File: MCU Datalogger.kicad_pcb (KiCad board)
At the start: 2 copper layers, 49.5 x 26.5 mm, 30 parts, among them J1 Conn_01x04_Pin, J2 Conn_01x04_Pin, J3 Conn_01x09_Pin, J4 Conn_02x03_Odd_Even, U1 24LC1025, U2 24LC1025, U3 DS1337S_, U4 ATMEGA328P-AU, Y1 16 MHz, Y2 32.768kHz

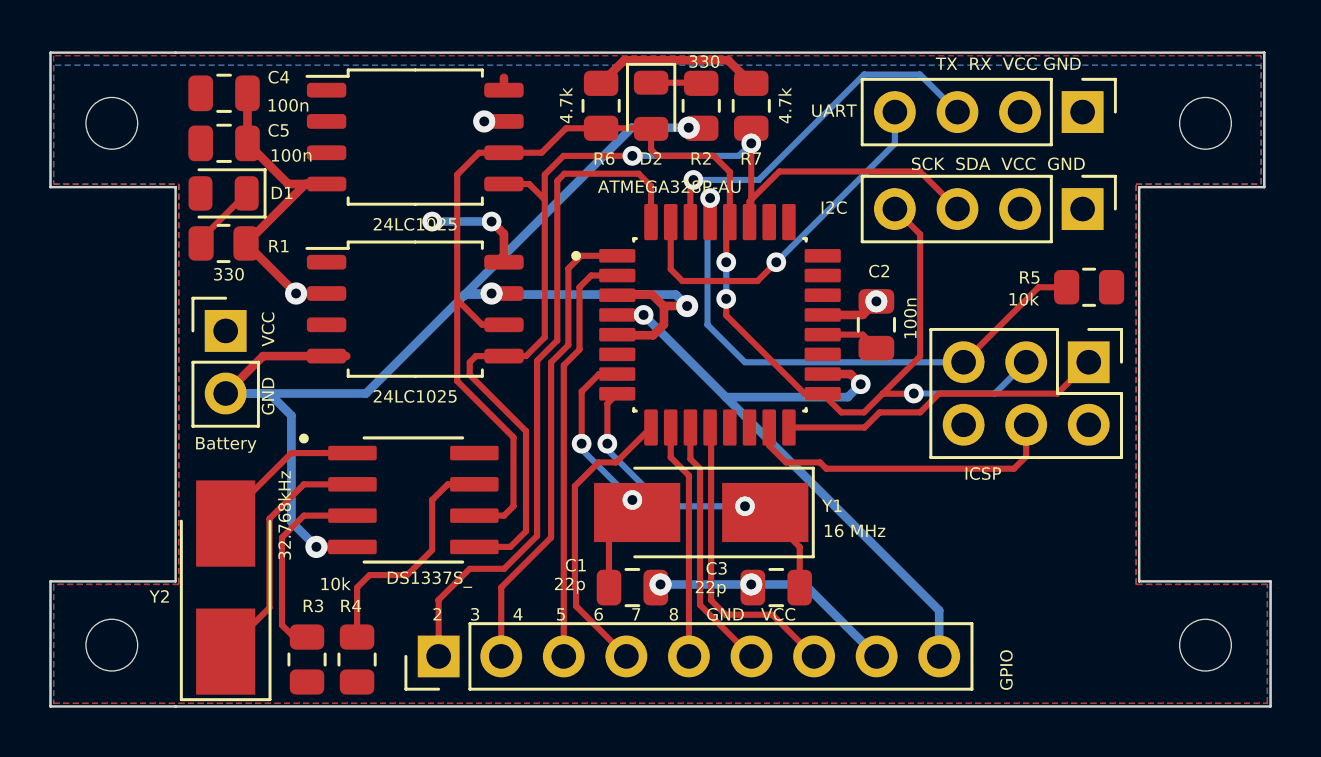
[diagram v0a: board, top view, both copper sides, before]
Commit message: 4-layer PCB completed
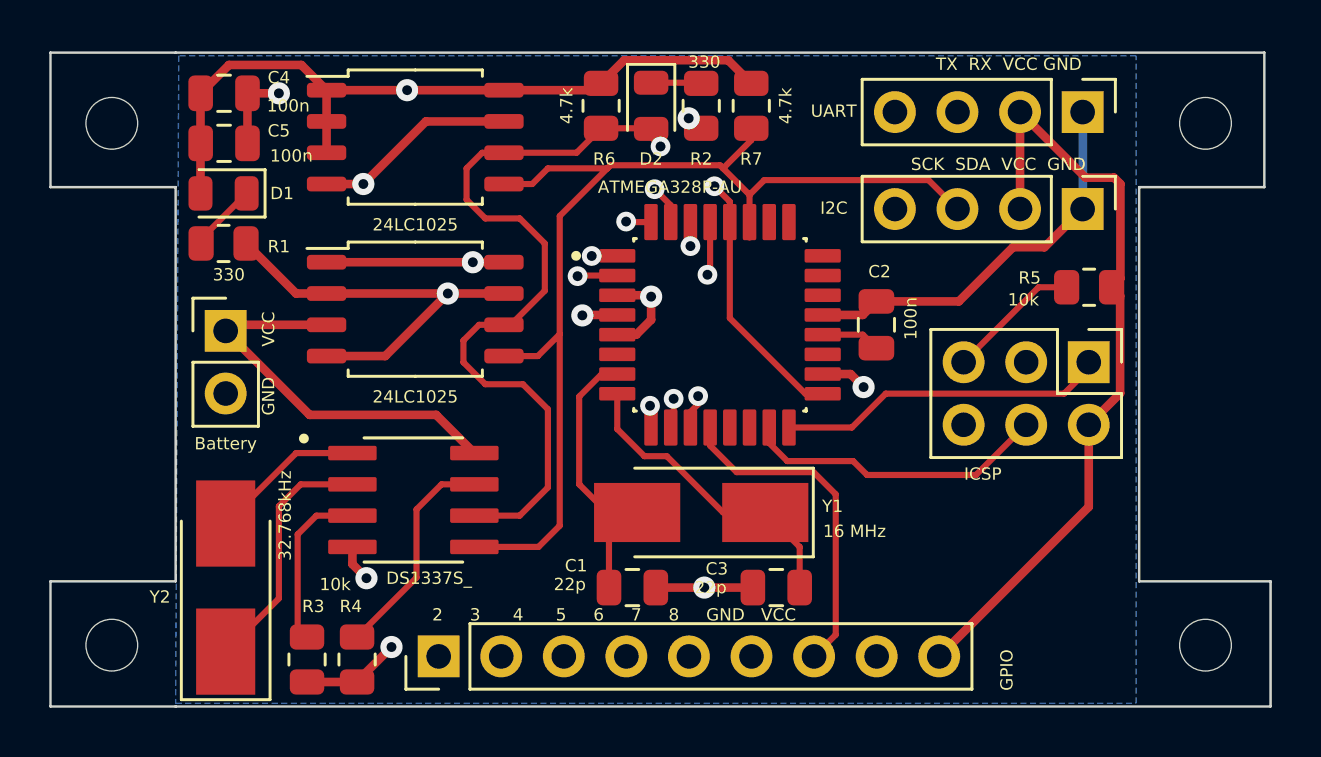
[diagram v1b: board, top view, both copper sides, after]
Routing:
- net /Vcc: track 39.5 -> 133.5 mm, vias 4 -> 5
- net GND: track 83.0 -> 55.2 mm, vias 9 -> 7
- net /D6: track 9.60 -> 17.0 mm, vias 0 -> 1
- net /D7: track 10.3 -> 17.2 mm, vias 0 -> 1
- net /D2: track 27.7 -> 23.0 mm, vias 0 -> 1
- net /D4: track 17.0 -> 20.9 mm, vias 0 -> 1
- net /RESET: track 22.0 -> 19.5 mm
- net /D3: track 19.1 -> 21.3 mm, vias 0 -> 1
- net /D5: track 11.9 -> 14.0 mm, vias 0 -> 1
- net /TX: track 14.8 -> 12.7 mm
- net /D8: track 12.2 -> 13.6 mm
- net /~{INTA}: track 8.00 -> 6.86 mm
- net Net-(U4-PB7): track 13.5 -> 12.5 mm, vias 2 -> 0
- net /SCK: track 60.6 -> 61.7 mm, vias 3 -> 2
- net /SQW: track 9.69 -> 8.95 mm
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- added copper zone on In2.Cu, net /Vcc
- removed copper zone on F.Cu, net /Vcc
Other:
- copper layers 2 -> 4

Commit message: board charasteristics added
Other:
- board text added: "4"
- board text removed: "2"
- board text removed: "Afterall, there are some clearence violations that must be corrected"
- board text removed: "CORRECTED"
- board text removed: "Unfortunately Vcc label is not defined as POWER net class so that Vcc track width was set as default (0.25mm). After the DRC process, the net class definitions checked and reorganized. Labels that entered by users should write with {dblquote}/{dblquote} prefix. For example /Vcc ."
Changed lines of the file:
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@@
       (drillshape 0)
       (scaleselection 1)
-      (outputdirectory "MCU_Datalogger_Gerbers/")
+      (outputdirectory "4_layer_MCU_Datalogger_Gerbers/")
     )
   )
@@
   (gr_line (start 123.952 76.454) (end 129.032 76.454)
     (stroke (width 0.1) (type default)) (layer "Edge.Cuts"))
-  (gr_rect (start 121.158 22.86) (end 194.818 47.371)
-    (stroke (width 0.15) (type default)) (fill none) (layer "User.1"))
   (gr_rect (start 129.00438 50.36596) (end 168.23842 76.42819)
     (stroke (width 0.1) (type default)) (fill none) (layer "User.1"))
@@
     (effects (font (size 0.5 0.5) (thickness 0.0625)) (justify left bottom))
   )
-  (gr_text "49.5300 mm x 26.5430 mm" (at 153.041143 104.447) (layer "User.1")
+  (gr_text "None" (at 142.113 106.192) (layer "User.1")
     (effects (font (size 1.5 1.5) (thickness 0.2)) (justify left top))
   )
-  (gr_text "None" (at 153.041143 112.361) (layer "User.1")
+  (gr_text "No" (at 142.113 114.106) (layer "User.1")
     (effects (font (size 1.5 1.5) (thickness 0.2)) (justify left top))
   )
-  (gr_text "No" (at 212.141138 116.318) (layer "User.1")
+  (gr_text "1.6000 mm" (at 201.212995 94.321) (layer "User.1")
     (effects (font (size 1.5 1.5) (thickness 0.2)) (justify left top))
   )
-  (gr_text "Copper Finish: " (at 120.384 112.361) (layer "User.1")
+  (gr_text "Board Thickness: " (at 176.270138 94.321) (layer "User.1")
     (effects (font (size 1.5 1.5) (thickness 0.2)) (justify left top))
   )
-  (gr_text "BOARD CHARACTERISTICS" (at 119.634 94.996) (layer "User.1")
-    (effects (font (size 2 2) (thickness 0.4)) (justify left top))
-  )
-  (gr_text "Unfortunately Vcc label is not defined as POWER net class\nso that Vcc track width was set as default (0.25mm). \nAfter the DRC process, the net class definitions checked and\nreorganized. \n\nLabels that entered by users should write with {dblquote}/{dblquote} prefix.\nFor example /Vcc ." (at 122.301 40.259) (layer "User.1")
-    (effects (font (size 1.5 1.5) (thickness 0.1875)) (justify left bottom))
-  )
-  (gr_text "" (at 187.198281 104.447) (layer "User.1")
+  (gr_text "0.3000 mm" (at 201.212995 102.235) (layer "User.1")
     (effects (font (size 1.5 1.5) (thickness 0.2)) (justify left top))
   )
-  (gr_text "Edge card connectors: " (at 120.384 120.275) (layer "User.1")
+  (gr_text "Min hole diameter: " (at 176.270138 102.235) (layer "User.1")
     (effects (font (size 1.5 1.5) (thickness 0.2)) (justify left top))
   )
-  (gr_text "Plated Board Edge: " (at 187.198281 116.318) (layer "User.1")
+  (gr_text "49.5300 mm x 26.5430 mm" (at 142.113 98.278) (layer "User.1")
     (effects (font (size 1.5 1.5) (thickness 0.2)) (justify left top))
   )
-  (gr_text "Copper Layer Count: " (at 120.384 100.49) (layer "User.1")
+  (gr_text "Impedance Control: " (at 176.270138 106.192) (layer "User.1")
     (effects (font (size 1.5 1.5) (thickness 0.2)) (justify left top))
   )
-  (gr_text "No" (at 212.141138 112.361) (layer "User.1")
+  (gr_text "0.2000 mm / 0.0000 mm" (at 142.113 102.235) (layer "User.1")
     (effects (font (size 1.5 1.5) (thickness 0.2)) (justify left top))
   )
-  (gr_text "0.3000 mm" (at 212.141138 108.404) (layer "User.1")
+  (gr_text "Plated Board Edge: " (at 176.270138 110.149) (layer "User.1")
     (effects (font (size 1.5 1.5) (thickness 0.2)) (justify left top))
   )
-  (gr_text "2" (at 153.041143 100.49) (layer "User.1")
+  (gr_text "" (at 201.212995 98.278) (layer "User.1")
     (effects (font (size 1.5 1.5) (thickness 0.2)) (justify left top))
   )
-  (gr_text "1.6000 mm" (at 212.141138 100.49) (layer "User.1")
+  (gr_text "Copper Layer Count: " (at 109.455857 94.321) (layer "User.1")
     (effects (font (size 1.5 1.5) (thickness 0.2)) (justify left top))
   )
-  (gr_text "Min track/spacing: " (at 120.384 108.404) (layer "User.1")
+  (gr_text "Min track/spacing: " (at 109.455857 102.235) (layer "User.1")
     (effects (font (size 1.5 1.5) (thickness 0.2)) (justify left top))
   )
-  (gr_text "No" (at 153.041143 120.275) (layer "User.1")
-    (effects (font (size 1.5 1.5) (thickness 0.2)) (justify left top))
+  (gr_text "BOARD CHARACTERISTICS" (at 108.705857 88.827) (layer "User.1")
+    (effects (font (size 2 2) (thickness 0.4)) (justify left top))
   )
-  (gr_text "Min hole diameter: " (at 187.198281 108.404) (layer "User.1")
+  (gr_text "No" (at 201.212995 106.192) (layer "User.1")
     (effects (font (size 1.5 1.5) (thickness 0.2)) (justify left top))
   )
-  (gr_text "" (at 212.141138 104.447) (layer "User.1")
+  (gr_text "Board overall dimensions: " (at 109.455857 98.278) (layer "User.1")
     (effects (font (size 1.5 1.5) (thickness 0.2)) (justify left top))
   )
-  (gr_text "No" (at 153.041143 116.318) (layer "User.1")
+  (gr_text "Castellated pads: " (at 109.455857 110.149) (layer "User.1")
     (effects (font (size 1.5 1.5) (thickness 0.2)) (justify left top))
   )
-  (gr_text "Impedance Control: " (at 187.198281 112.361) (layer "User.1")
+  (gr_text "" (at 176.270138 98.278) (layer "User.1")
     (effects (font (size 1.5 1.5) (thickness 0.2)) (justify left top))
   )
-  (gr_text "Afterall, there are some clearence violations that must be \ncorrected" (at 122.174 44.958) (layer "User.1")
-    (effects (font (size 1.5 1.5) (thickness 0.1875)) (justify left bottom))
-  )
-  (gr_text "Board Thickness: " (at 187.198281 100.49) (layer "User.1")
+  (gr_text "No" (at 142.113 110.149) (layer "User.1")
     (effects (font (size 1.5 1.5) (thickness 0.2)) (justify left top))
   )
-  (gr_text "Castellated pads: " (at 120.384 116.318) (layer "User.1")
+  (gr_text "Copper Finish: " (at 109.455857 106.192) (layer "User.1")
     (effects (font (size 1.5 1.5) (thickness 0.2)) (justify left top))
   )
-  (gr_text "Board overall dimensions: " (at 120.384 104.447) (layer "User.1")
+  (gr_text "Edge card connectors: " (at 109.455857 114.106) (layer "User.1")
     (effects (font (size 1.5 1.5) (thickness 0.2)) (justify left top))
   )
-  (gr_text "0.2000 mm / 0.0000 mm" (at 153.041143 108.404) (layer "User.1")
+  (gr_text "No" (at 201.212995 110.149) (layer "User.1")
     (effects (font (size 1.5 1.5) (thickness 0.2)) (justify left top))
   )
-  (gr_text "CORRECTED" (at 152.146 46.101) (layer "User.2")
-    (effects (font (size 2 2) (thickness 0.2) bold) (justify left bottom))
+  (gr_text "4" (at 142.113 94.321) (layer "User.1")
+    (effects (font (size 1.5 1.5) (thickness 0.2)) (justify left top))
   )
   (gr_text_box "MISO | VCC\nSCK  | MOSI\nRES  | GND"
@@
     )
   )
-  (group "group-boardCharacteristics" (id 95389eac-e105-4d2f-8c4c-09d30f25d41b)
+  (group "group-boardCharacteristics" (id d3bed512-1df1-436e-bb04-f65a27582389)
     (members
-      05674f4c-808a-4519-80d6-cf5ebf1739f7
-      0abac70c-79c5-4807-8098-07bd74e61d0f
-      11765ced-6771-41f8-a889-852b2da5df73
-      19a3acfd-cba4-4bdc-9bb4-fcfb274f2648
-      291b5920-3a39-4a7d-9975-22e30d6dcf32
-      4394afd7-a3b4-4846-bb21-89a7c9821445
-      540214f1-3724-4a84-b9e1-49801215309a
-      587befab-c80d-4773-9af6-69a286fbc1b7
-      5d63a35f-5553-4bbe-a883-ab182b3f450c
-      61096dcd-609e-47f4-b811-e4bb4c122fdb
-      6a711cc7-0368-4578-bde5-27929309a136
-      6f164682-db31-4e58-9f2b-dd8bc67857ff
-      7ce9ce5c-39a7-4055-893d-cf5025cb74f3
-      84ec65fd-599f-495a-94c1-4b96a92f2973
-      941e0785-f8a0-49ed-b55d-2de885f64738
-      972bd823-1a0a-403b-ba49-ae7681676c4d
-      a45d8d05-74ed-4cfa-b06c-57f21bc49524
-      b4ebba8f-b497-4e47-9fe9-d7fa7f90111a
-      be51174a-7700-4ee4-beef-159280f1a6d1
-      c563acaf-5598-4c2a-959d-3ddabe4dba9b
-      ee071bb2-1f34-4c7f-968f-4989cf715d24
-      f2a075e7-9772-44a5-a5c5-8f46d42a64a6
-      f32e16bc-2e8a-4153-a9a3-afb381f3ab0e
+      053b8d61-d2ab-423f-bb51-9ae0f87e0792
+      09e06355-6296-461f-9283-cd0b065becc2
+      152ae82c-e924-47a9-a572-c238dd1852d9
+      2146eff6-833e-4a99-a55c-fc226f477f6f
+      2c5f5934-f184-4460-9690-dffe5448065f
+      42c87443-5591-4c92-a021-139843d54acd
+      4958b7b0-a167-405b-b182-5cffe41f292d
+      5519cf65-d711-469c-b414-b3bd4f15f1a7
+      6db5259a-5c98-4bc3-9a5b-cfa5d49ac6e6
+      7b780be9-4875-4350-9dac-7745316db5c7
+      7b9349f3-64f3-47ee-93d3-95d0a9a45647
+      870842c7-d4d8-4c57-8894-7b54bfd5c573
+      87c68f78-d6ba-4bf6-b7a6-5bec64dae799
+      8f42db29-c1b3-4050-9820-30cecd76eff8
+      96c2a3fa-fcff-49d4-8928-b4750b05046b
+      a640a3f2-b854-48c2-a9d6-1ab868b4b561
+      a7eafcf7-30b4-46d6-bd76-606f7e26b083
+      c7d1b28d-a863-461f-9a40-a41155a5c0ea
+      cf2e504d-38dd-47ba-a0b1-2b752c04e6cb
+      d4bbc8e7-4451-4884-9eb3-7b6bbf8128f3
+      de3c9567-82a2-4952-b7de-4479e4082f82
+      e00f3761-cdcc-4053-81e5-782e99e9d190
+      fecd5115-e7d5-41c2-8355-0c5b5ce3738a
     )
   )

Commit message: abc123 label fixed
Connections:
- net Net-(D2-K) renamed /abc123
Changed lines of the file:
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@@
   (net 5 "/Vcc")
   (net 6 "Net-(D1-K)")
-  (net 7 "Net-(D2-K)")
+  (net 7 "/abc123")
   (net 8 "/SCK")
   (net 9 "/SDA")
@@
       (stroke (width 0.1) (type solid)) (layer "F.Fab"))
     (pad "1" smd roundrect (at -0.9375 0 270) (size 0.975 1.4) (layers "F.Cu" "F.Paste" "F.Mask") (roundrect_rratio 0.25)
-      (net 7 "Net-(D2-K)") (pinfunction "K") (pintype "passive"))
+      (net 7 "/abc123") (pinfunction "K") (pintype "passive"))
     (pad "2" smd roundrect (at 0.9375 0 270) (size 0.975 1.4) (layers "F.Cu" "F.Paste" "F.Mask") (roundrect_rratio 0.25)
       (net 8 "/SCK") (pinfunction "A") (pintype "passive"))
@@
       (net 1 "GND") (pintype "passive"))
     (pad "2" smd roundrect (at 0.9125 0 90) (size 1.025 1.4) (layers "F.Cu" "F.Paste" "F.Mask") (roundrect_rratio 0.243902439)
-      (net 7 "Net-(D2-K)") (pintype "passive"))
+      (net 7 "/abc123") (pintype "passive"))
     (model "${KICAD6_3DMODEL_DIR}/Resistor_SMD.3dshapes/R_0805_2012Metric.wrl"
       (offset (xyz 0 0 0))

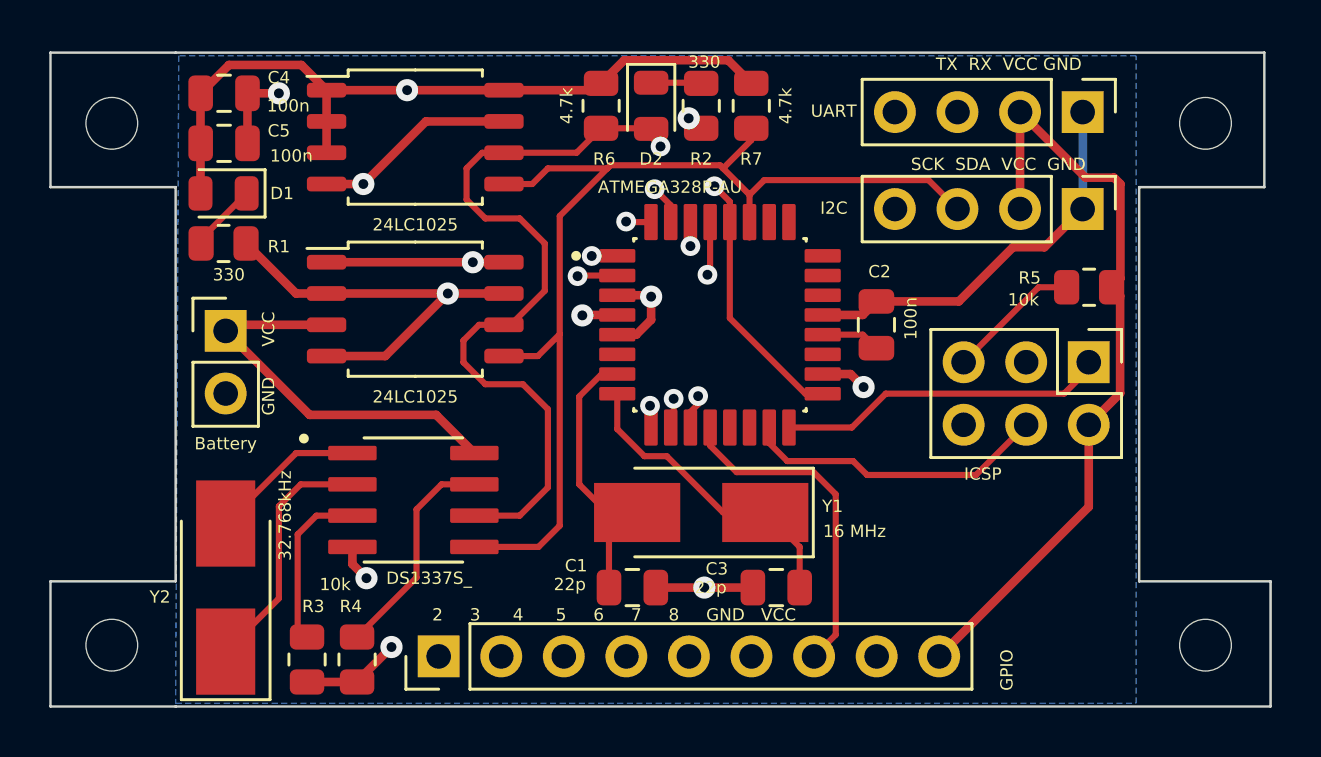
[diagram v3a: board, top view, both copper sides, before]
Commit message: Fixed net bugs in 4 layer PCB
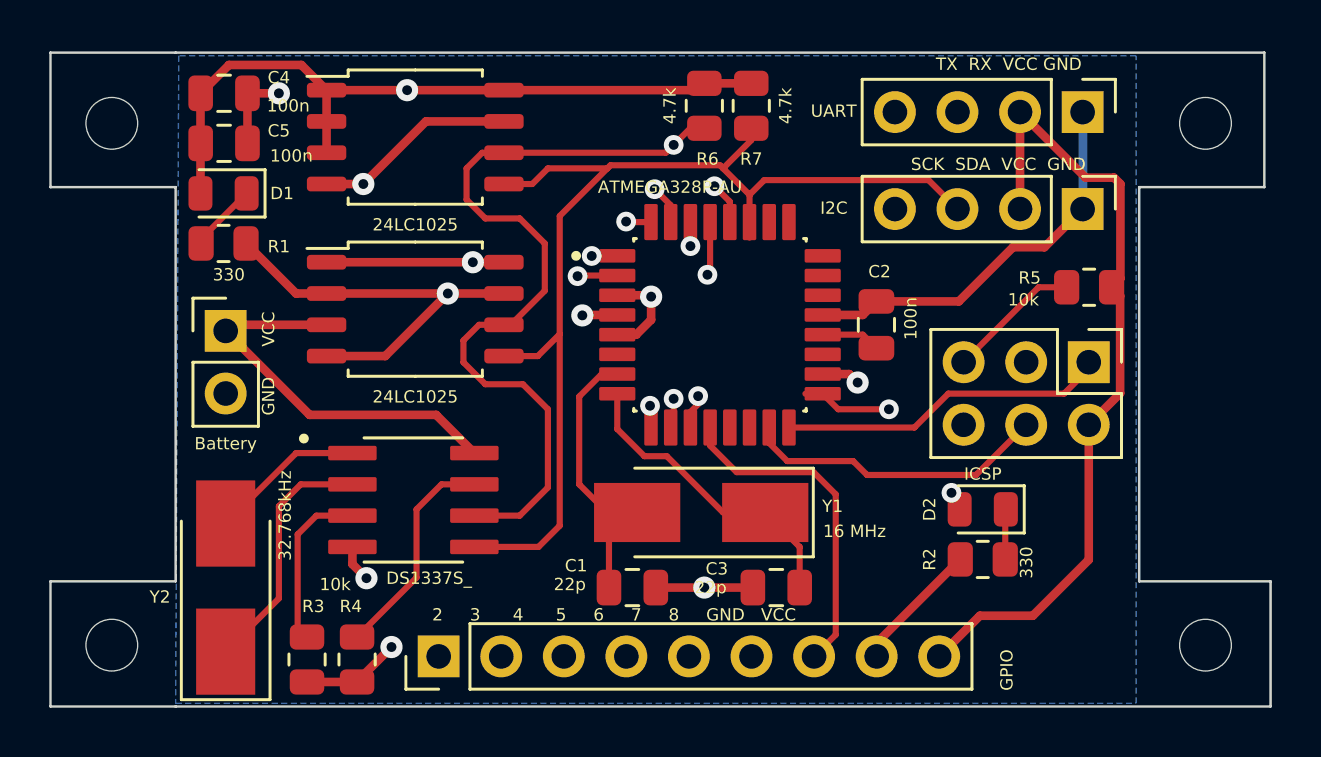
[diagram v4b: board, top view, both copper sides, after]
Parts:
- moved R2 21.7 mm to (161.8, 70.5), turned to 0 degrees
- moved D2 21.2 mm to (161.8, 68.5), turned to 180 degrees
- moved R6 4.19 mm to (150.5, 52.1)
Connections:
- J1 pad 4: /SCK -> /SCL
- R6 pad 2: /SCK -> /SCL
- U1 pad 6: /SCK -> /SCL
- U2 pad 6: /SCK -> /SCL
- U3 pad 6: /SCK -> /SCL
- U4 pad 28: /SCK -> /SCL
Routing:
- net /SCK: track 61.7 -> 15.3 mm
- net /SCL: track 0.00 -> 45.1 mm, vias 0 -> 2
- net GND: track 55.2 -> 59.9 mm, vias 7 -> 6
